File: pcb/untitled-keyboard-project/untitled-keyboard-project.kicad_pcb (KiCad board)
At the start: 2 copper layers, 65 parts, among them J1 USB_mini_micro_B, J2 AudioJack4, K1 KEYSW, K10 KEYSW, K11 KEYSW, K12 KEYSW, K13 KEYSW, K14 KEYSW, K15 KEYSW, K16 KEYSW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

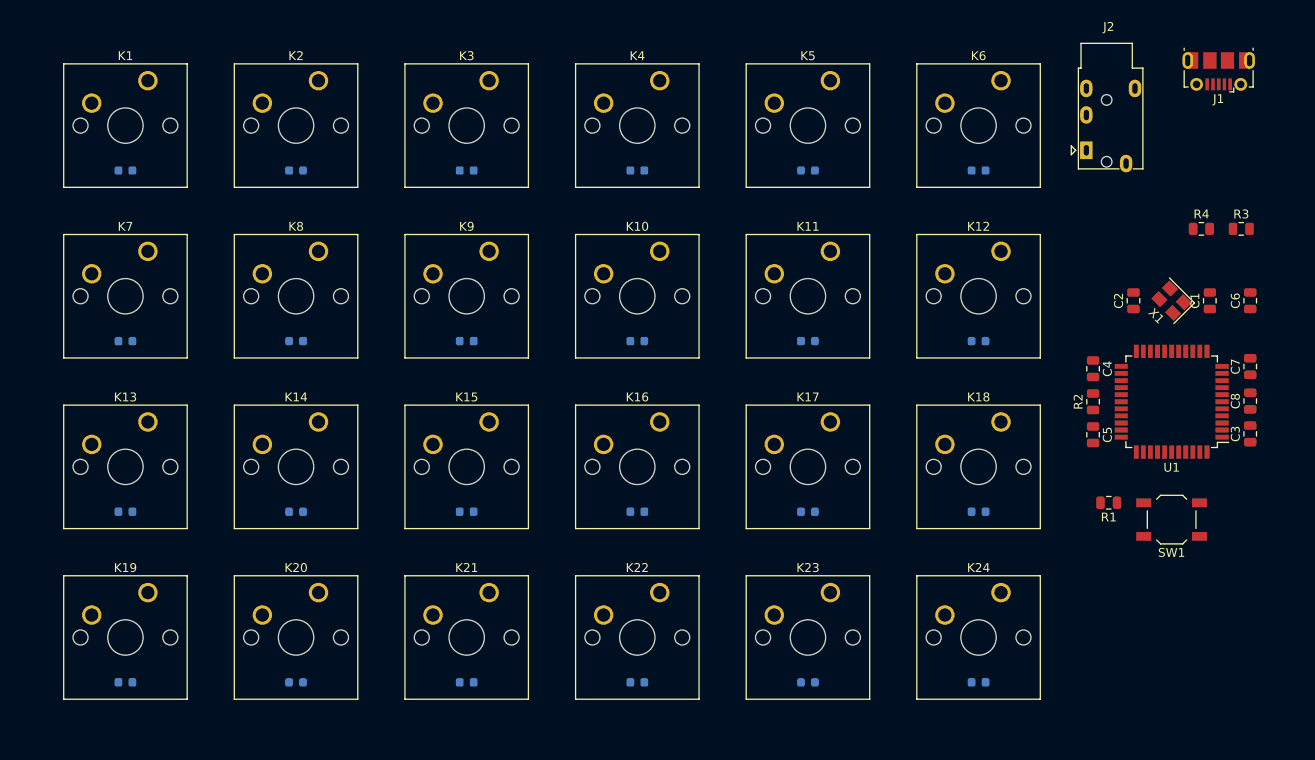
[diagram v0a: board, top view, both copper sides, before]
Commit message: Finished layout for Rev 0 board
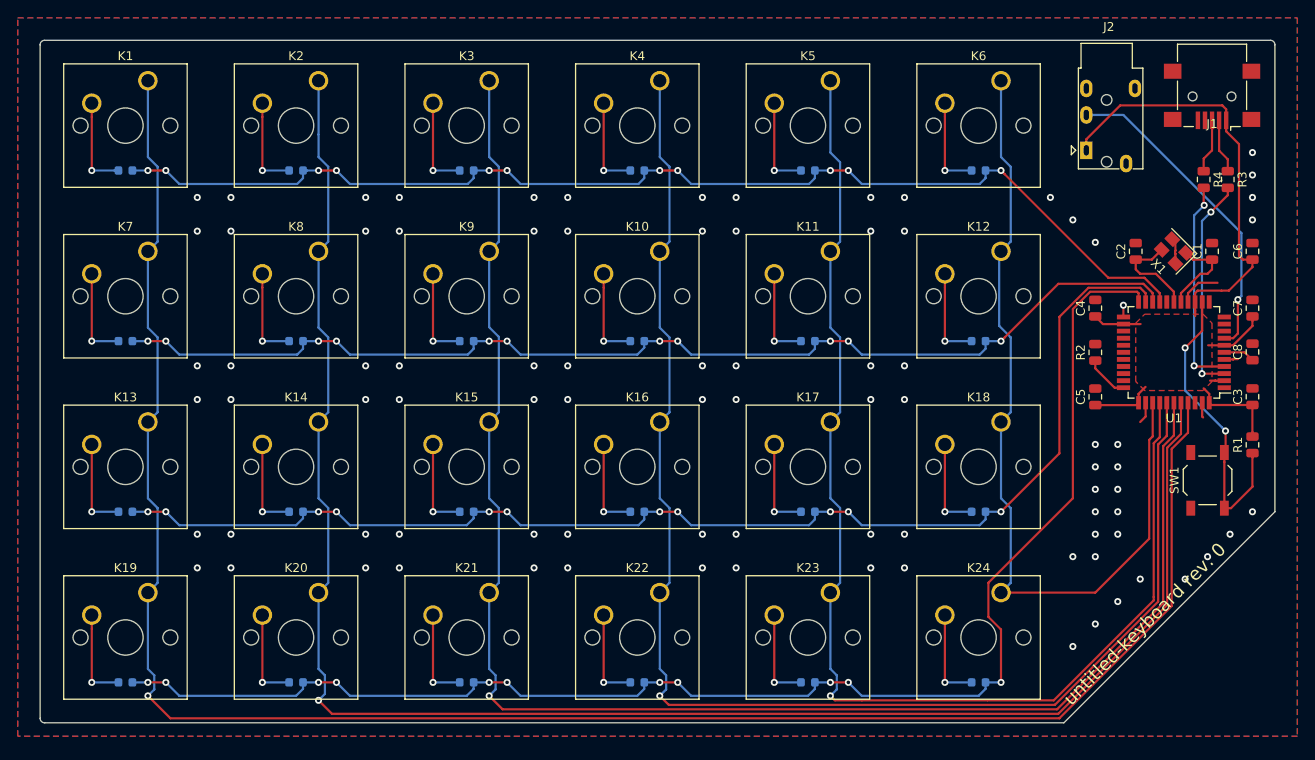
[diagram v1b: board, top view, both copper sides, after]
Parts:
- J1: value USB_mini_micro_B -> USB_mini_B; footprint Connector_USB:USB_Micro-B_Molex-105017-0001 -> Connector_USB:USB_Mini-B_Lumberg_2486_01_Horizontal
- moved R1 17.5 mm to (200.7, 86.4), turned to 90 degrees
- moved C4 6.86 mm to (182.9, 70.9), turned to 90 degrees
- moved C7 6.61 mm to (200.7, 70.9)
- moved SW1 6.02 mm to (195.6, 90.4), turned to 90 degrees
- moved R3 5.79 mm to (197.9, 56.4), turned to 270 degrees
- moved U1 5.59 mm to (191.8, 75.9)
- moved R2 5.59 mm to (182.9, 75.9)
- moved R4 5.59 mm to (195.1, 56.4), turned to 270 degrees
- moved X1 5.59 mm to (191.8, 64.5)
- moved C1 5.59 mm to (196.1, 64.5)
- moved C2 5.59 mm to (187.5, 64.5)
- moved C6 5.59 mm to (200.7, 64.5)
- moved C8 5.56 mm to (200.7, 75.9)
- moved C5 4.30 mm to (182.9, 81.0), turned to 90 degrees
- moved C3 4.21 mm to (200.7, 81.0)
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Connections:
- net Net-(R1-Pad1) renamed /reset
- U1 pad 19: Net-(U1-Pad19) -> /row1
- U1 pad 20: Net-(U1-Pad20) -> /row2
- U1 pad 21: Net-(U1-Pad21) -> /row3
- U1 pad 22: Net-(U1-Pad22) -> /row4
- U1 pad 29: /row4 -> Net-(U1-Pad29)
- U1 pad 30: /row3 -> Net-(U1-Pad30)
- U1 pad 31: /row2 -> Net-(U1-Pad31)
- U1 pad 32: /row1 -> Net-(U1-Pad32)
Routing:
- net /col1: track 0.00 -> 218.8 mm, vias 0 -> 1
- net /col2: track 0.00 -> 198.7 mm, vias 0 -> 1
- net /col3: track 0.00 -> 178.0 mm, vias 0 -> 1
- net /row4: track 0.00 -> 162.8 mm, vias 0 -> 11
- net /col4: track 0.00 -> 157.5 mm, vias 0 -> 1
- net /row3: track 0.00 -> 144.1 mm, vias 0 -> 11
- net /col5: track 0.00 -> 137.0 mm, vias 0 -> 1
- net /row1: track 0.00 -> 132.1 mm, vias 0 -> 11
- net /row2: track 0.00 -> 128.3 mm, vias 0 -> 11
- net /col6: track 0.00 -> 95.7 mm
- net VUSB: track 0.00 -> 80.6 mm
- net /serial: track 0.00 -> 36.4 mm, vias 0 -> 1
- net /reset: track 0.00 -> 34.2 mm, vias 0 -> 2
- net Net-(R3-Pad2): track 0.00 -> 24.8 mm, vias 0 -> 2
- net Net-(R4-Pad2): track 0.00 -> 24.1 mm, vias 0 -> 2
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- added copper zone on B.Cu, net GNDREF
- added copper zone on F.Cu, net GNDREF
- added copper zone on F.Cu, net VUSB
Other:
- board outline added: 139.7 x 77.2 mm
- board text added: "untitled-keyboard rev. 0"

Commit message: Update 11/28/2020
Capacitor Value Change
File Cleanup
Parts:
- C1, C2: value 22pF -> 18pF
- J1: value USB_mini_B -> USB_mini_micro_B
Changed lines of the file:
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@@
       (effects (font (size 1 1) (thickness 0.15)))
     )
-    (fp_text value 22pF (at 0 1.65 270) (layer F.Fab)
+    (fp_text value 18pF (at 0 1.65 270) (layer F.Fab)
       (effects (font (size 1 1) (thickness 0.15)))
     )
@@
       (effects (font (size 1 1) (thickness 0.15)))
     )
-    (fp_text value 22pF (at 0 1.65 270) (layer F.Fab)
+    (fp_text value 18pF (at 0 1.65 270) (layer F.Fab)
       (effects (font (size 1 1) (thickness 0.15)))
     )
@@
       (effects (font (size 1 1) (thickness 0.15)))
     )
-    (fp_text value USB_mini_B (at 0.3 4.3375) (layer F.Fab)
+    (fp_text value USB_mini_micro_B (at 0.3 4.3375) (layer F.Fab)
       (effects (font (size 1 1) (thickness 0.15)))
     )
@@
   (segment (start 200.66 84.9835) (end 200.66 81.9) (width 0.25) (layer F.Cu) (net 4))
   (segment (start 200.66 85.471) (end 200.66 84.9835) (width 0.25) (layer F.Cu) (net 4))
-  (segment (start 199.771 75.946) (end 197.47 75.946) (width 0.25) (layer F.Cu) (net 5))
-  (segment (start 200.66 76.835) (end 199.771 75.946) (width 0.25) (layer F.Cu) (net 5))
-  (segment (start 196.088 49.69) (end 196.088 53.086) (width 0.25) (layer F.Cu) (net 34))
-  (segment (start 195.138 54.036) (end 195.138 55.4505) (width 0.25) (layer F.Cu) (net 34))
-  (segment (start 196.088 53.086) (end 195.138 54.036) (width 0.25) (layer F.Cu) (net 34))
-  (segment (start 196.888 49.69) (end 196.888 53.124) (width 0.25) (layer F.Cu) (net 36))
-  (segment (start 197.866 54.102) (end 197.866 55.4505) (width 0.25) (layer F.Cu) (net 36))
-  (segment (start 196.888 53.124) (end 197.866 54.102) (width 0.25) (layer F.Cu) (net 36))
-  (segment (start 185.07 79.946) (end 186.07 79.946) (width 0.25) (layer F.Cu) (net 45))
-  (segment (start 182.88 76.8835) (end 182.88 77.756) (width 0.25) (layer F.Cu) (net 45))
-  (segment (start 182.88 77.756) (end 185.07 79.946) (width 0.25) (layer F.Cu) (net 45))
   (segment (start 196.024 81.9) (end 195.77 81.646) (width 0.25) (layer F.Cu) (net 4))
   (segment (start 200.66 81.9) (end 196.024 81.9) (width 0.25) (layer F.Cu) (net 4))
@@
   (segment (start 187.77 80.646) (end 188.5696 79.8464) (width 0.25) (layer F.Cu) (net 4))
   (segment (start 187.77 81.646) (end 187.77 80.646) (width 0.25) (layer F.Cu) (net 4))
+  (segment (start 199.771 75.946) (end 197.47 75.946) (width 0.25) (layer F.Cu) (net 5))
+  (segment (start 200.66 76.835) (end 199.771 75.946) (width 0.25) (layer F.Cu) (net 5))
   (segment (start 72.3645 55.372) (end 71.927 55.372) (width 0.25) (layer B.Cu) (net 6))
   (via (at 69.342 55.372) (size 0.8) (drill 0.4) (layers F.Cu B.Cu) (net 6))
@@
   (segment (start 168.8845 113.284) (end 165.862 113.284) (width 0.25) (layer B.Cu) (net 33))
   (segment (start 165.862 105.664) (end 165.862 113.284) (width 0.25) (layer F.Cu) (net 33))
+  (segment (start 196.088 49.69) (end 196.088 53.086) (width 0.25) (layer F.Cu) (net 34))
+  (segment (start 195.138 54.036) (end 195.138 55.4505) (width 0.25) (layer F.Cu) (net 34))
+  (segment (start 196.088 53.086) (end 195.138 54.036) (width 0.25) (layer F.Cu) (net 34))
+  (segment (start 196.888 49.69) (end 196.888 53.124) (width 0.25) (layer F.Cu) (net 36))
+  (segment (start 197.866 54.102) (end 197.866 55.4505) (width 0.25) (layer F.Cu) (net 36))
+  (segment (start 196.888 53.124) (end 197.866 54.102) (width 0.25) (layer F.Cu) (net 36))
   (via (at 199.009 69.977) (size 0.8) (drill 0.4) (layers F.Cu B.Cu) (net 38))
   (segment (start 199.009 73.807) (end 199.009 69.977) (width 0.25) (layer F.Cu) (net 38))
@@
   (segment (start 173.311999 74.251999) (end 173.311999 82.720001) (width 0.25) (layer B.Cu) (net 44))
   (segment (start 171.997001 64.730999) (end 171.997001 72.937001) (width 0.25) (layer B.Cu) (net 44))
+  (segment (start 185.07 79.946) (end 186.07 79.946) (width 0.25) (layer F.Cu) (net 45))
+  (segment (start 182.88 76.8835) (end 182.88 77.756) (width 0.25) (layer F.Cu) (net 45))
+  (segment (start 182.88 77.756) (end 185.07 79.946) (width 0.25) (layer F.Cu) (net 45))
   (segment (start 197.866 57.3255) (end 197.866 57.813) (width 0.25) (layer F.Cu) (net 46))
   (via (at 195.961 60.071) (size 0.8) (drill 0.4) (layers F.Cu B.Cu) (net 46))
